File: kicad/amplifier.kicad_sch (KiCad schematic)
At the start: 21 parts, among them U9 GS8332-SR

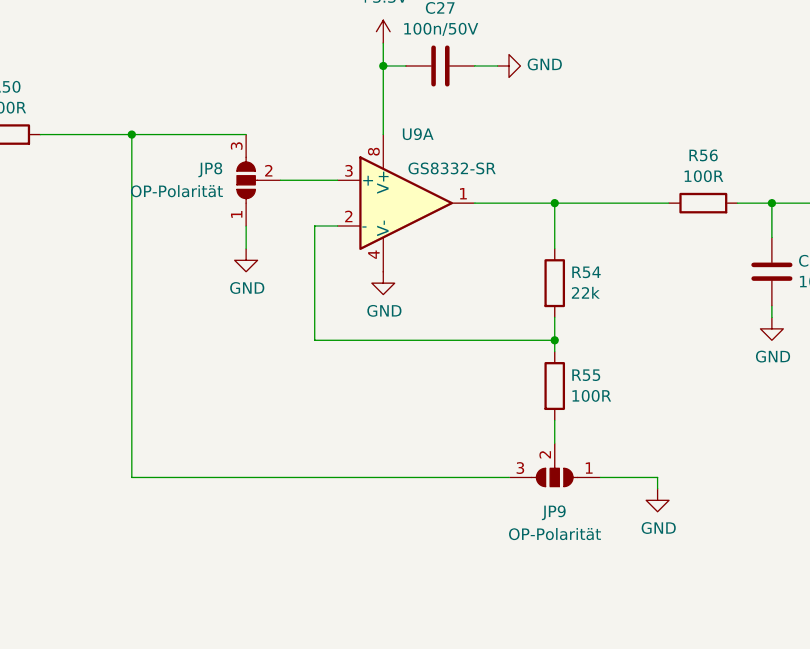
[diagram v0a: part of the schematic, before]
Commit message: created bom for order lcsc
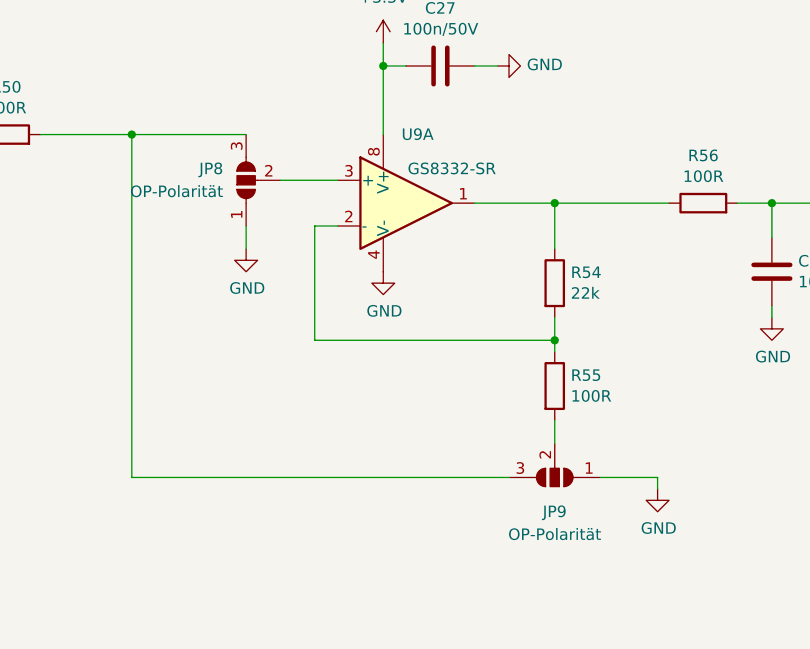
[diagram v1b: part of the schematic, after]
